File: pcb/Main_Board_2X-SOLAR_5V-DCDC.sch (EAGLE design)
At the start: 29 parts, among them T2 MMUN2133LT1G, U1 LTC4015EUHFPBFQFN-38_UHF-M, U3 TPS61090RSAR, X1 6V_PV, X2 5V output

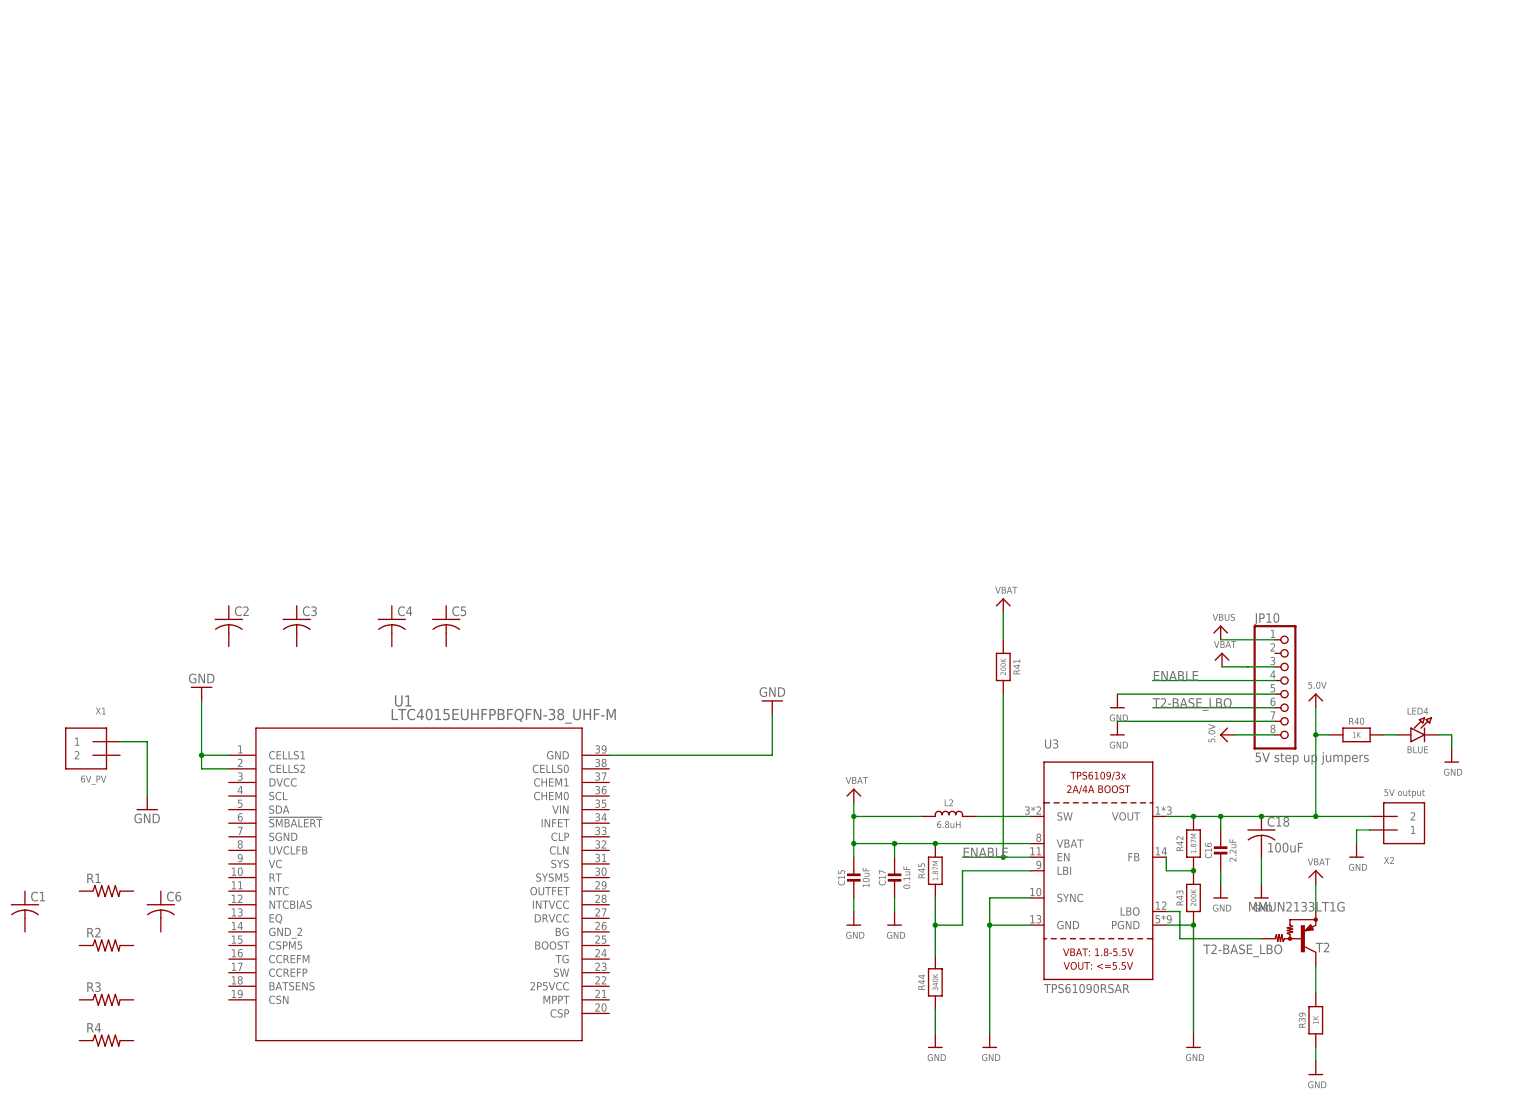
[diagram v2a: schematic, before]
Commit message: Updated BOM and layout for LTC4015
Schematic pinout redone for LTC4015 part to match design application guide and make schematic easier to follow. Schematic and board routing started. BOM updated and consolidated for last revision of board (non-LTC)
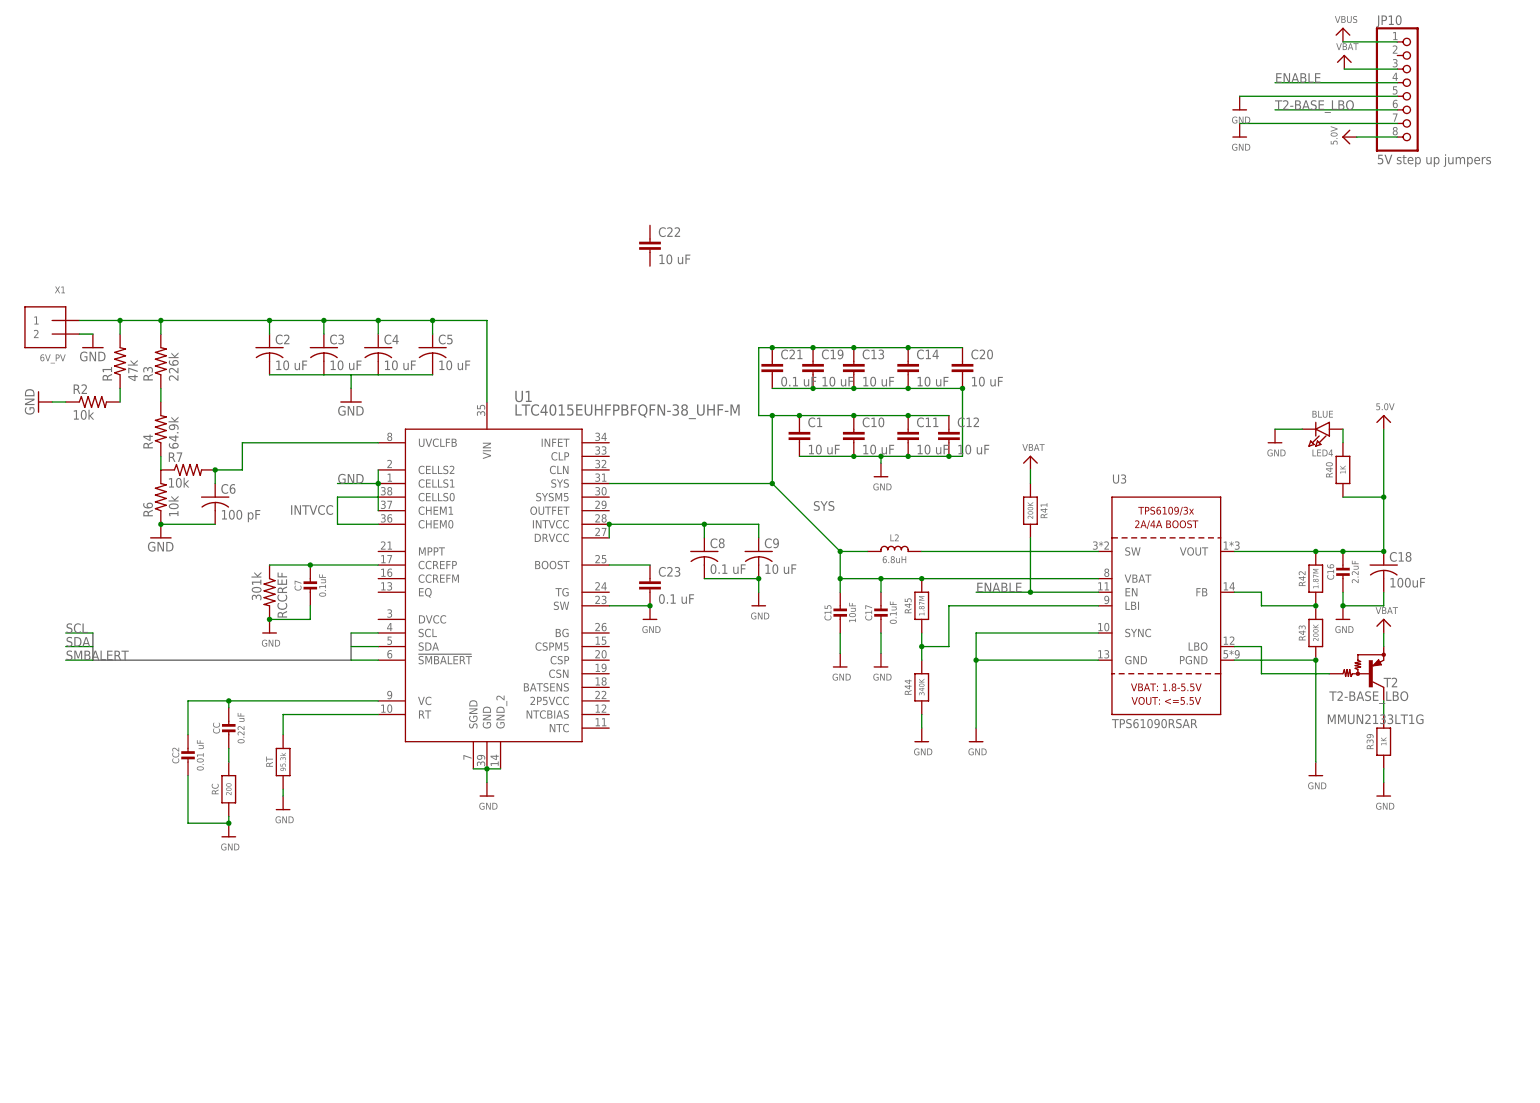
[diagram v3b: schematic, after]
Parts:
- removed X2: 5V output, microbuilder:TERMBLOCK_1X2
- added C10, C11, C12, C13, C14, C19, C20, C22: 10 uF, resistor:C-EUC1206
- added C21, C23: 0.1 uF, resistor:C-EUC1206
- added C7: 0.1uF, microbuilder:CAP_CERAMIC0805_10MGAP
- added C8: 0.1 uF, adafruit:C-USC0805
- added C9: 10 uF, adafruit:C-USC0805
- added CC: 0.22 uF, microbuilder:CAP_CERAMIC0805-NOOUTLINE
- added CC2: 0.01 uF, microbuilder:CAP_CERAMIC0805-NOOUTLINE
- added R6, R7: 10k, adafruit:R-US_R0805
- added RC: 200, microbuilder:RESISTOR0805_NOOUTLINE
- added RCCREF: 301k, adafruit:R-US_R0805
- added RT: 95.3k, microbuilder:RESISTOR0805_NOOUTLINE
- C1: value (none) -> 10 uF; device adafruit:C-USC0805 -> resistor:C-EUC1206
- C2, C3, C4, C5: value (none) -> 10 uF
- C6: value (none) -> 100 pF
- R1: value (none) -> 47k
- R2: value (none) -> 10k
- R3: value (none) -> 226k
- R4: value (none) -> 64.9k
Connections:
- net N$42 renamed FB
- net N$44 renamed LED+
- new net INTVCC: C8.1, C9.1, U1.CELLS0, U1.CHEM0, U1.DRVCC, U1.INTVCC
- new net N$1: C6.1, R7.2, U1.UVCLFB
- new net N$11: CC.2, RC.2
- new net N$12: C23.1, U1.BOOST
- new net N$2: C2.1, C3.1, C4.1, C5.1, R1.2, R3.2, U1.VIN, X1.1
- new net N$3: R3.1, R4.2
- new net N$4: R4.1, R6.2, R7.1
- new net N$5: R1.1, R2.2
- new net N$6: C7.1, RCCREF.1, U1.CCREFP
- new net N$8: RT.2, U1.RT
- new net N$9: CC.1, CC2.1, U1.VC
- new net SCL: U1.SCL
- new net SDA: U1.SDA
- new net SMBALERT: U1.!SMBALERT
- new net SYS: C1.1, C10.1, C11.1, C12.1, C13.1, C14.1, C15.1, C17.1, C19.1, C20.1, C21.1, L2.1, R45.2, U1.SYS, U3.VBAT
- net 5.0V: no longer X2.2
- net GND: now also C1.2, C10.2, C11.2, C12.2, C13.2, C14.2, C19.2, C2.2, C20.2, C21.2, C23.2, C3.2, C4.2, C5.2, C6.2, C7.2, C8.2, C9.2, CC2.2, R2.1, R6.1, RC.1, RCCREF.2, RT.1, U1.CHEM1, U1.GND_2, U1.SGND, U1.SW, X1.2; no longer X1.1, X2.1
- net VBAT: no longer C15.1, C17.1, L2.1, R45.2, U3.VBAT
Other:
- moved on the sheet: C1, C15, C16, C17, C18, C2, C3, C4, C5, C6, JP10, L2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

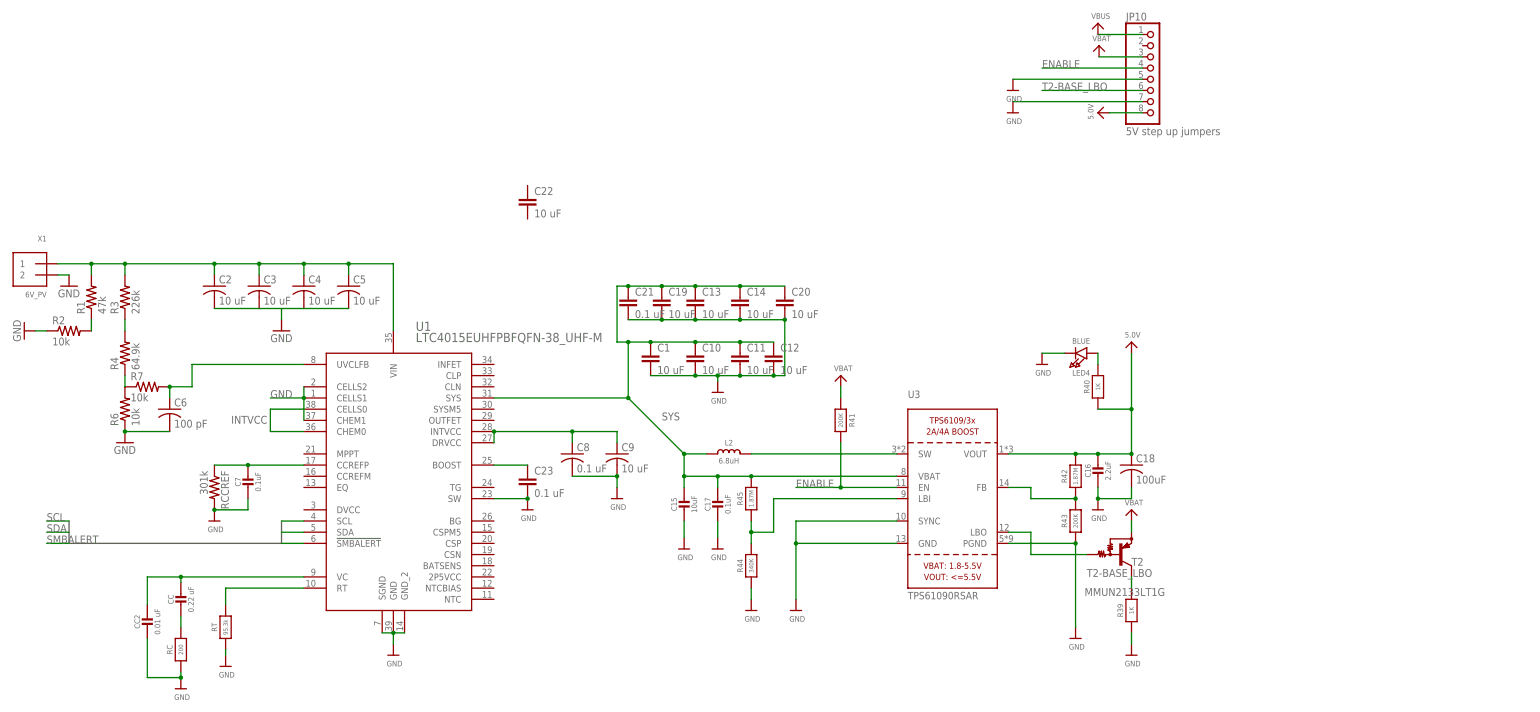
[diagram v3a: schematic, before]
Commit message: Updated library, schematic, and board layout
Added new components to library and continuing to update schematic and board
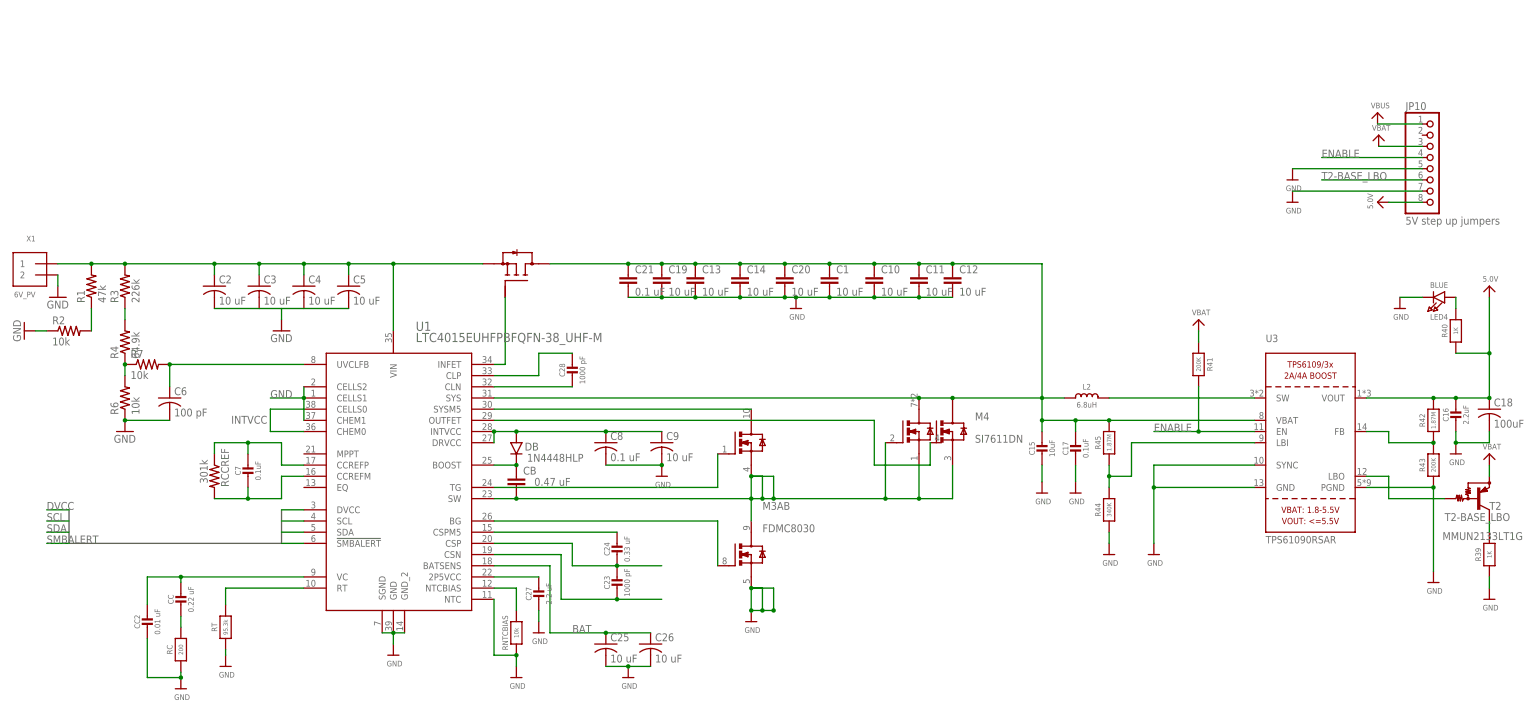
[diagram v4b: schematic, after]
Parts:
- removed C22: 10 uF, resistor:C-EUC1206
- added C24: 0.33 uF, microbuilder:CAP_CERAMIC0805-NOOUTLINE
- added C25, C26: 10 uF, adafruit:C-USC1206
- added C27: 2.2 uF, microbuilder:CAP_CERAMIC0805-NOOUTLINE
- added C28: 1000 pF, microbuilder:CAP_CERAMIC0805-NOOUTLINE
- added CB: 0.47 uF, resistor:C-EUC1206
- added DB: 1N4448HLP, RCT:1N4448HLP
- added M3AB: FDMC8030, FDMC8030:FDMC8030
- added M4: SI7611DN, Si7611DN:SI7611DN
- added M5: FDMC8327L, RCT:FDMC8327L
- added RNTCBIAS: 10k, microbuilder:RESISTOR_0805MP
- C23: value 0.1 uF -> 1000 pF; device resistor:C-EUC1206 -> microbuilder:CAP_CERAMIC0805-NOOUTLINE
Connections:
- net N$1 renamed UVCLFB
- new net BAT: C25.1, C26.1, U1.BATSENS
- new net BG: M3AB.G2, U1.BG
- new net CSN: C23.2, U1.CSN
- new net CSP: C23.1, C24.2, U1.CSP
- new net CSPM5: C24.1, U1.CSPM5
- new net DVCC: U1.DVCC
- new net INFET: M5.GATE, U1.INFET
- new net N$10: RNTCBIAS.2, U1.NTCBIAS
- new net N$13: CB.1, DB.P$1, U1.BOOST
- new net N$14: C28.2, U1.CLN
- new net N$15: C28.1, U1.CLP
- new net N$7: C27.1, U1.2P5VCC
- new net OUTFET: M4.G2, U1.OUTFET
- new net SYSM5_DRAIN_2: M3AB.D1, U1.SYSM5
- new net TG: M3AB.G1, U1.TG
- new net VIN: C2.1, C3.1, C4.1, C5.1, M5.SOURCE, R1.2, R3.2, U1.VIN, X1.1
- net GND: now also C25.2, C26.2, C27.2, M3AB.S2, RNTCBIAS.1, U1.NTC; no longer C23.2, C7.2, RCCREF.2, U1.SW
- net INTVCC: now also DB.P$2
- net N$12: now also CB.2, M3AB.D2, M3AB.S1, M4.G1, M4.S1, M4.S2, U1.SW; no longer C23.1, U1.BOOST
- net N$2: now also C7.2, RCCREF.2, U1.CCREFM; no longer C2.1, C3.1, C4.1, C5.1, R1.2, R3.2, U1.VIN, X1.1
- net SYS: now also M4.D1, M4.D2, M5.DRAIN
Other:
- moved on the sheet: C1, C10, C11, C12, C13, C14, C15, C16, C17, C18, C19, C20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

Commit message: New BOM for LiFePO4 board and updated sch/brd
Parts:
- removed R1: 47k, adafruit:R-US_R0805
- removed R2, R7: 10k, adafruit:R-US_R0805
- removed R4: 64.9k, adafruit:R-US_R0805
- added FRAME1: FRAME-LEDGER, SparkFun-Aesthetics:FRAME-LEDGER
- added RSNS: KRL3216T4A-M-R004-F-T1, RCT:KRL3216T4A-M-R004-F-T1
- added U$4: XAL1010-103ME-103ME, RCT:XAL1010-103ME-103ME
- R3: value 226k -> 200k
- R6: value 10k -> 50k
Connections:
- net N$7 renamed 2P5VCC
- removed net N$3: R3.1, R4.2
- removed net N$4: R4.1, R6.2, R7.1
- removed net N$5: R1.1, R2.2
- new net EQ: U1.EQ
- new net N$1: M4.G1, M4.S1, M4.S2, U$4.P$2
- net GND: now also U1.MPPT; no longer R2.1
- net N$12: now also U$4.P$1; no longer M4.G1, M4.S1, M4.S2
- net UVCLFB: now also R3.1, R6.2; no longer R7.2
- net VIN: no longer R1.2
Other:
- moved on the sheet: C6, R3, R6, RNTCBIAS
